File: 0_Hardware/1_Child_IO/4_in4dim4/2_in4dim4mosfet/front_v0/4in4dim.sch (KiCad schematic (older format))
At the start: 37 parts, among them IC1 ATTINY48-A, P1 CONN_8X2, P2 CONN_2, P3 CONN_2, P4 CONN_2, P5 CONN_2, Q1 PNP, Q2 PNP, Q3 PNP, Q4 PNP

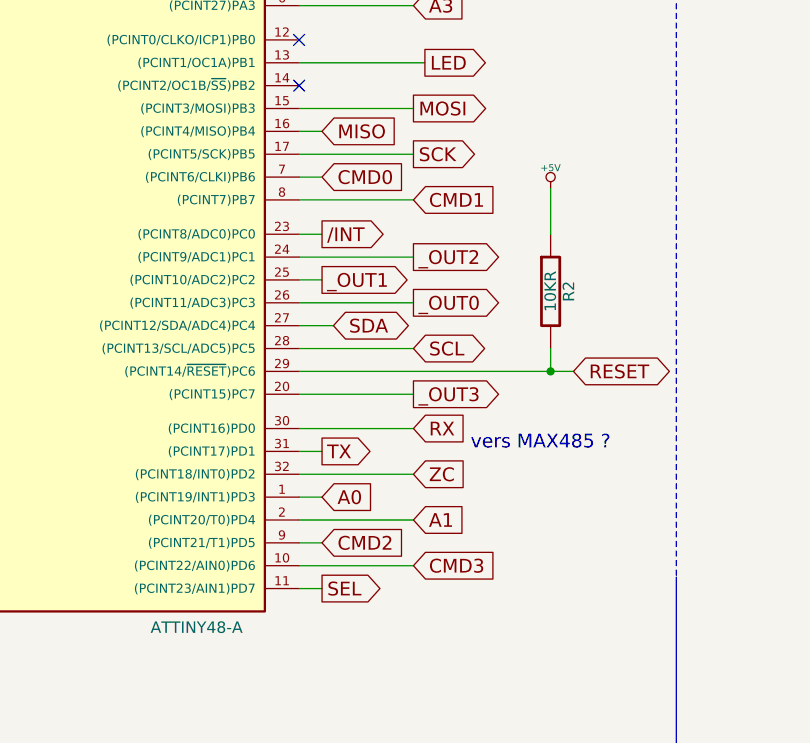
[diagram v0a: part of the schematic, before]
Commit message: Mise à jour du PCB Front Panel in4dim4mosfet   -> Inversion des broches dans le schéma pour faciliter le routage        * CMD0 Broche7 => Broche 10 de l'attiny        * CMD1 Broche8 => Broche 9 de l'attiny        * CMD2 Broche9 => Broche 8 de l'attiny        * CMD3 Broche10 => Broche 8 de l'attiny   -> Changement des types de led pour D2 à D9 (Transverse en CMS)   -> Mise en place des plan de masse des deux côtés
Mise à jour nom dans les gerber SMB V0.0 pour éviter les pb Smartgit
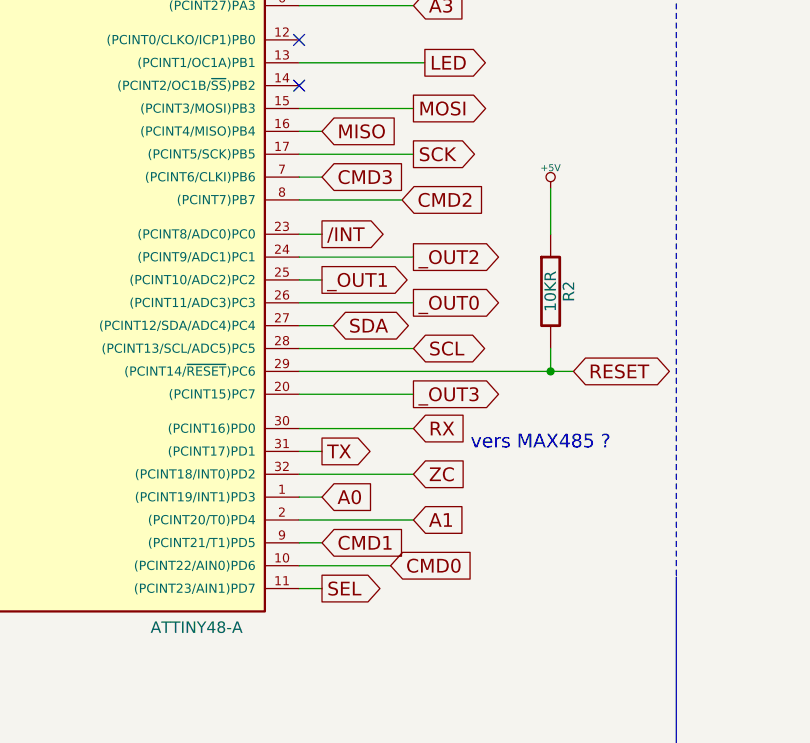
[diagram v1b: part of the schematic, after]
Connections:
- net CMD0: now also IC1.10 ((PCINT22/AIN0)PD6); no longer IC1.7 ((PCINT6/CLKI)PB6)
- net CMD1: now also IC1.9 ((PCINT21/T1)PD5); no longer IC1.8 ((PCINT7)PB7)
- net CMD2: now also IC1.8 ((PCINT7)PB7); no longer IC1.9 ((PCINT21/T1)PD5)
- net CMD3: now also IC1.7 ((PCINT6/CLKI)PB6); no longer IC1.10 ((PCINT22/AIN0)PD6)
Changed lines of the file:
@@
 	1    0    0    -1
 $EndComp
-Text GLabel 8100 9700 2    60   Input ~ 0
+Text GLabel 8400 11400 2    60   Input ~ 0
 CMD0
 Text GLabel 8150 10350 2    60   BiDi ~ 0
@@
 	1    0    0    -1
 $EndComp
+Text GLabel 8450 9800 2    60   Input ~ 0
+CMD2
 Text GLabel 8100 11300 2    60   Input ~ 0
-CMD2
-Text GLabel 8500 9800 2    60   Input ~ 0
 CMD1
-Text GLabel 8500 11400 2    60   Input ~ 0
+Text GLabel 8100 9700 2    60   Input ~ 0
 CMD3
 NoConn ~ 8000 9300
@@
 Connection ~ 6100 8650
 Wire Wire Line
-	8000 11400 8500 11400
-Wire Wire Line
-	8000 11300 8100 11300
-Wire Wire Line
 	8000 11200 8500 11200
 Wire Wire Line
@@
 Wire Wire Line
 	8000 10150 8100 10150
-Wire Wire Line
-	8000 9800 8500 9800
-Wire Wire Line
-	8000 9700 8100 9700
 Wire Wire Line
 	8000 9600 8500 9600
@@
 	1    0    0    -1
 $EndComp
+Wire Wire Line
+	8000 9700 8100 9700
+Wire Wire Line
+	8000 9800 8450 9800
+Wire Wire Line
+	8000 11300 8100 11300
+Wire Wire Line
+	8000 11400 8400 11400
 $EndSCHEMATC

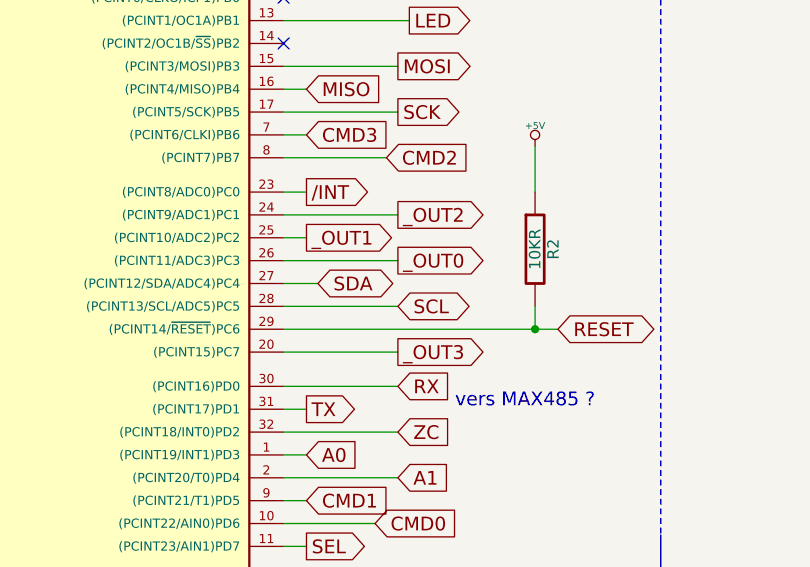
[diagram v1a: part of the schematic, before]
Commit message: Mise à jour du Front Panel in4dim4 mosfet
- Ecartement des composants
- Inversion des broches de sorties de l'attinye OUT0 à 4 pour faciliter le routage
- Ajout de la sérigraphie
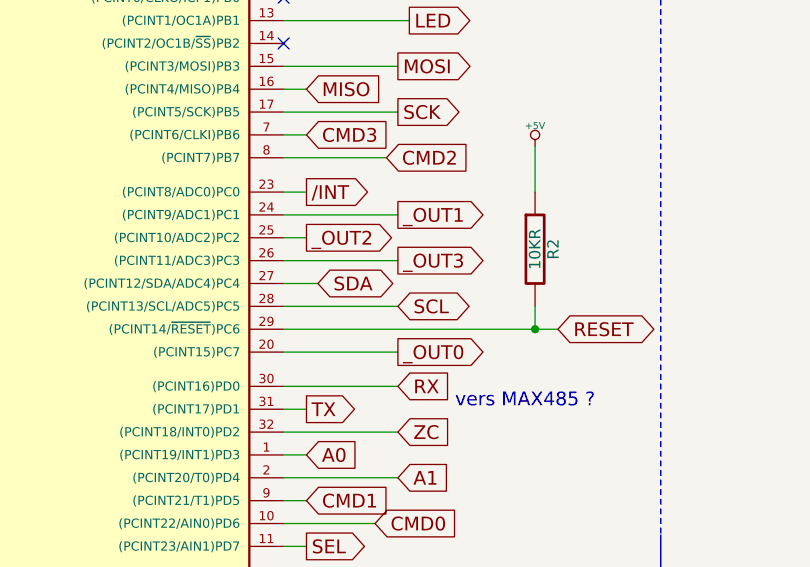
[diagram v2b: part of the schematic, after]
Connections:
- net _OUT0: now also IC1.20 ((PCINT15)PC7); no longer IC1.26 ((PCINT11/ADC3)PC3)
- net _OUT1: now also IC1.24 ((PCINT9/ADC1)PC1); no longer IC1.25 ((PCINT10/ADC2)PC2)
- net _OUT2: now also IC1.25 ((PCINT10/ADC2)PC2); no longer IC1.24 ((PCINT9/ADC1)PC1)
- net _OUT3: now also IC1.26 ((PCINT11/ADC3)PC3); no longer IC1.20 ((PCINT15)PC7)
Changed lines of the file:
@@
 	1    0    0    -1
 $EndComp
+Text GLabel 8500 10250 2    60   Output ~ 0
+_OUT3
+Text GLabel 8100 10150 2    60   Output ~ 0
+_OUT2
 Text GLabel 8500 10650 2    60   Output ~ 0
-_OUT3
+_OUT0
 Text GLabel 8500 10050 2    60   Output ~ 0
-_OUT2
-Text GLabel 8500 10250 2    60   Output ~ 0
-_OUT0
-Text GLabel 8100 10150 2    60   Output ~ 0
 _OUT1
 Text GLabel 8500 9400 2    60   Output ~ 0
@@
 	8000 10350 8150 10350
 Wire Wire Line
-	8000 10150 8100 10150
-Wire Wire Line
 	8000 9600 8500 9600
 Wire Wire Line
@@
 Wire Wire Line
 	7200 4850 7200 4800
-Wire Wire Line
-	8000 10050 8500 10050
-Wire Wire Line
-	8000 10250 8500 10250
-Wire Wire Line
-	8000 10650 8500 10650
 Wire Wire Line
 	8000 9950 8100 9950
@@
 Wire Wire Line
 	8000 11400 8400 11400
+Wire Wire Line
+	8000 10050 8500 10050
+Wire Wire Line
+	8000 10150 8100 10150
+Wire Wire Line
+	8000 10250 8500 10250
+Wire Wire Line
+	8000 10650 8500 10650
 $EndSCHEMATC

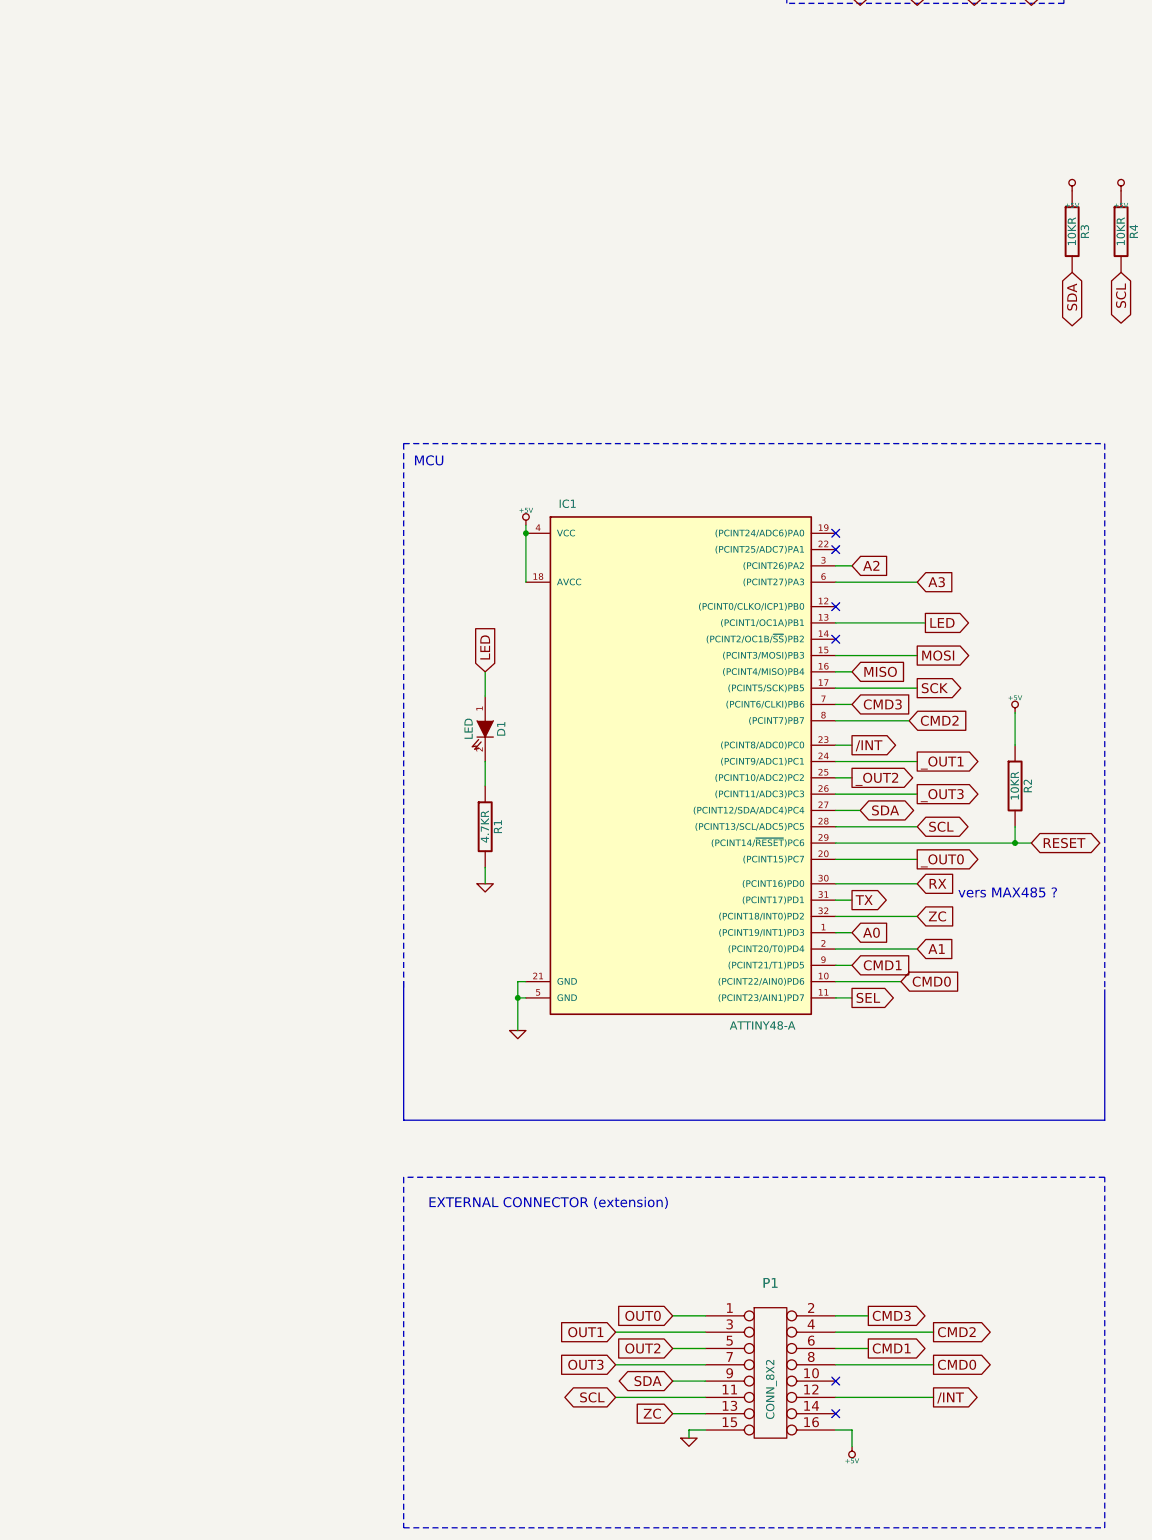
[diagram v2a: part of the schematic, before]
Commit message: mis à jour de la carte de puissance et de la front panel
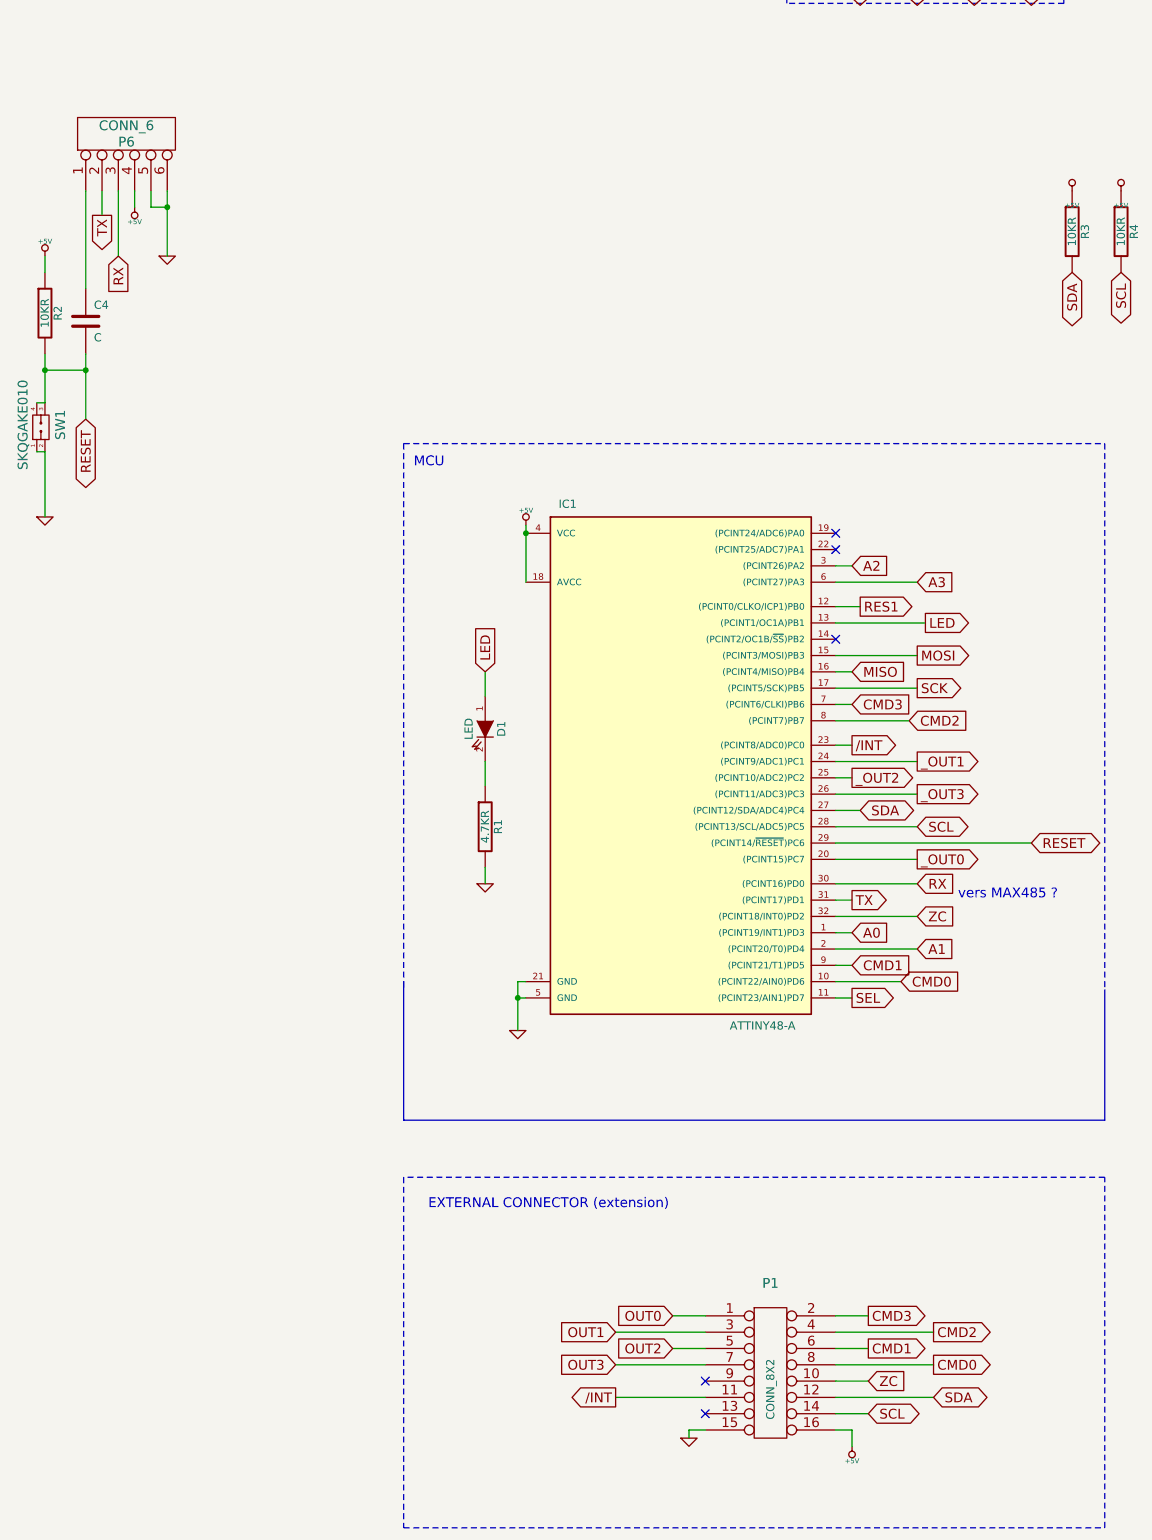
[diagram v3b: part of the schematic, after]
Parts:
- added C4: C, symbol C
- added P6: CONN_6, symbol CONN_6
- added SW1: SKQGAKE010, symbol SKQGAKE010
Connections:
- net +5V: now also P6.4
- net /INT: now also P1.11; no longer P1.12
- net GND: now also P6.5, P6.6, SW1.1, SW1.2
- net RESET: now also C4.2, SW1.3, SW1.4
- net RX: now also P6.3
- net SCL: now also P1.14; no longer P1.11
- net SDA: now also P1.12; no longer P1.9
- net TX: now also P6.2
- net ZC: now also P1.10; no longer P1.13
- net RES1: now reaches IC1.12 ((PCINT0/CLKO/ICP1)PB0)
- new net: C4.1, P6.1
- no-connect marks 6 -> 5
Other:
- moved on the sheet: R2

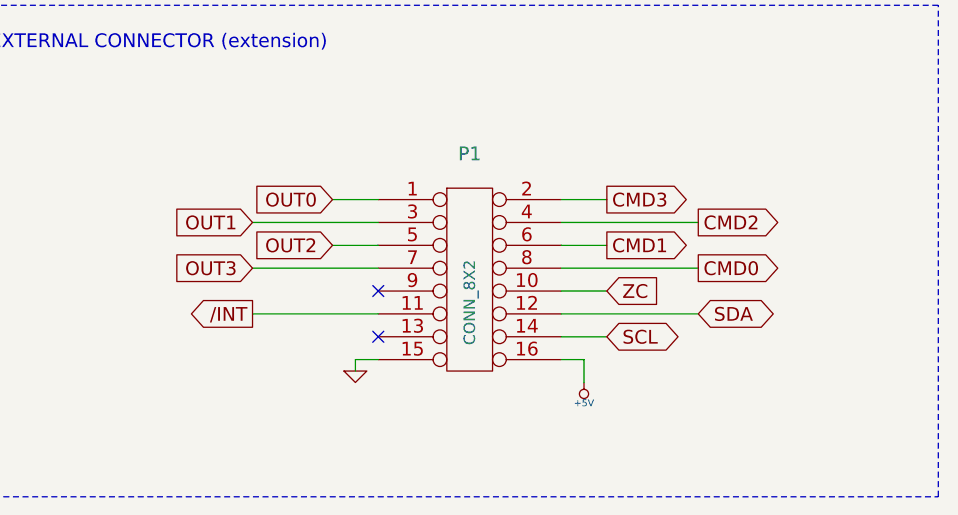
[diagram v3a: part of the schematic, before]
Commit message: Front panel dimmer: - passé tous les composants sauf leds et bouton reset face dessous pour libérer la place pour la sérigraphie - suite modif pinout connecteur 20 pins côté puissance - reroutage (TODO: à optimiser)
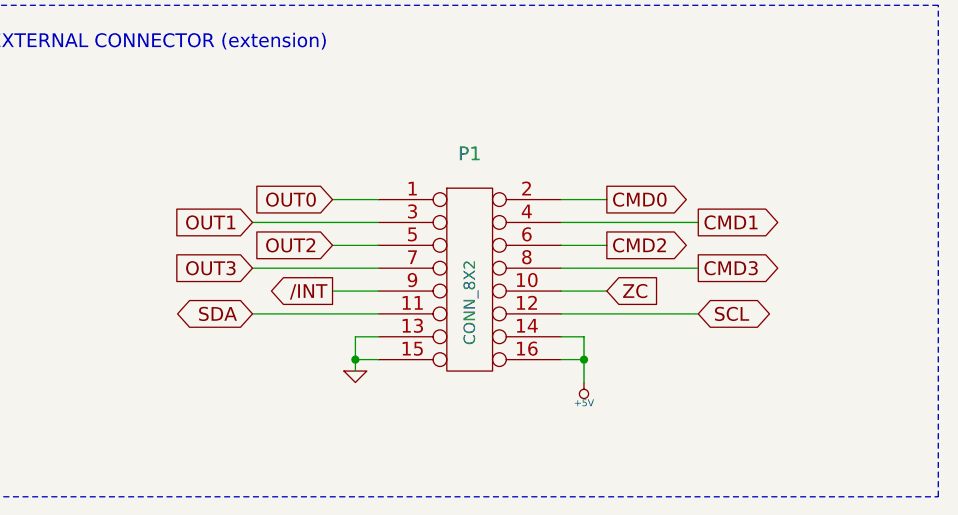
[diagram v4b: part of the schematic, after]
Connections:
- net +5V: now also P1.14
- net /INT: now also P1.9; no longer P1.11
- net CMD0: now also P1.2; no longer P1.8
- net CMD1: now also P1.4; no longer P1.6
- net CMD2: now also P1.6; no longer P1.4
- net CMD3: now also P1.8; no longer P1.2
- net GND: now also P1.13
- net SCL: now also P1.12; no longer P1.14
- net SDA: now also P1.11; no longer P1.12
- no-connect marks 5 -> 3
